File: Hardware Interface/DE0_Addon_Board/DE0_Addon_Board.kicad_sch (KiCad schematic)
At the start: 5 parts, among them J1 Conn_02x20_Odd_Even, J3 Raspberry PI GPIO, U1 IS61WV25616EDBLL

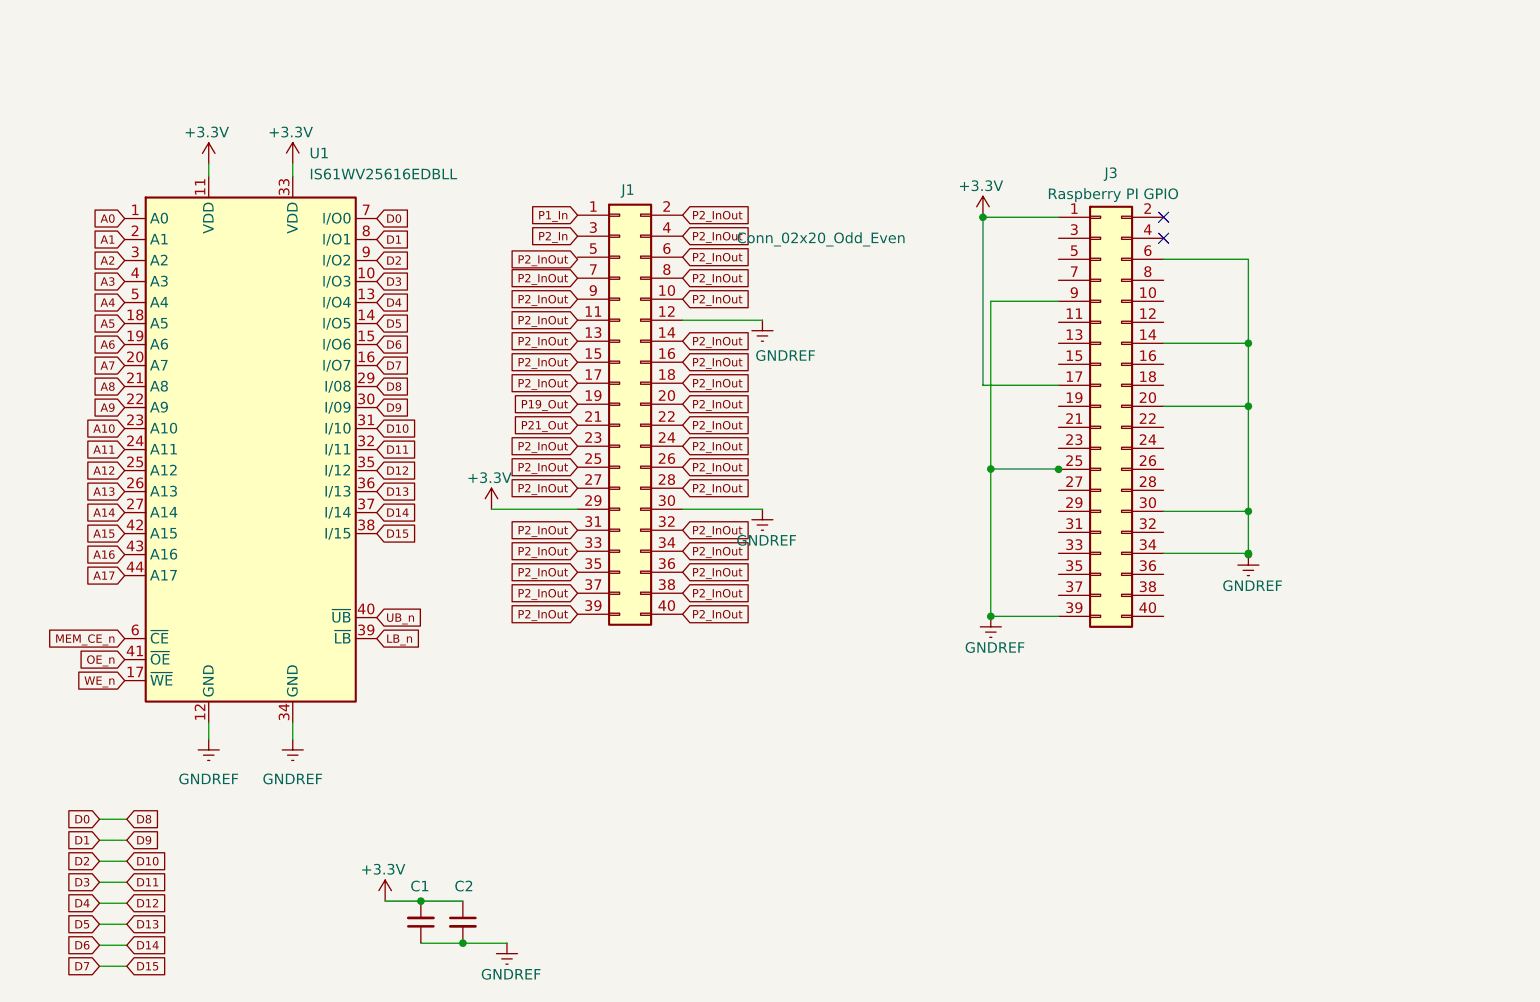
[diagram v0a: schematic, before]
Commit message: Addon-board changed to support Raspberry Pi in the GPIO connector
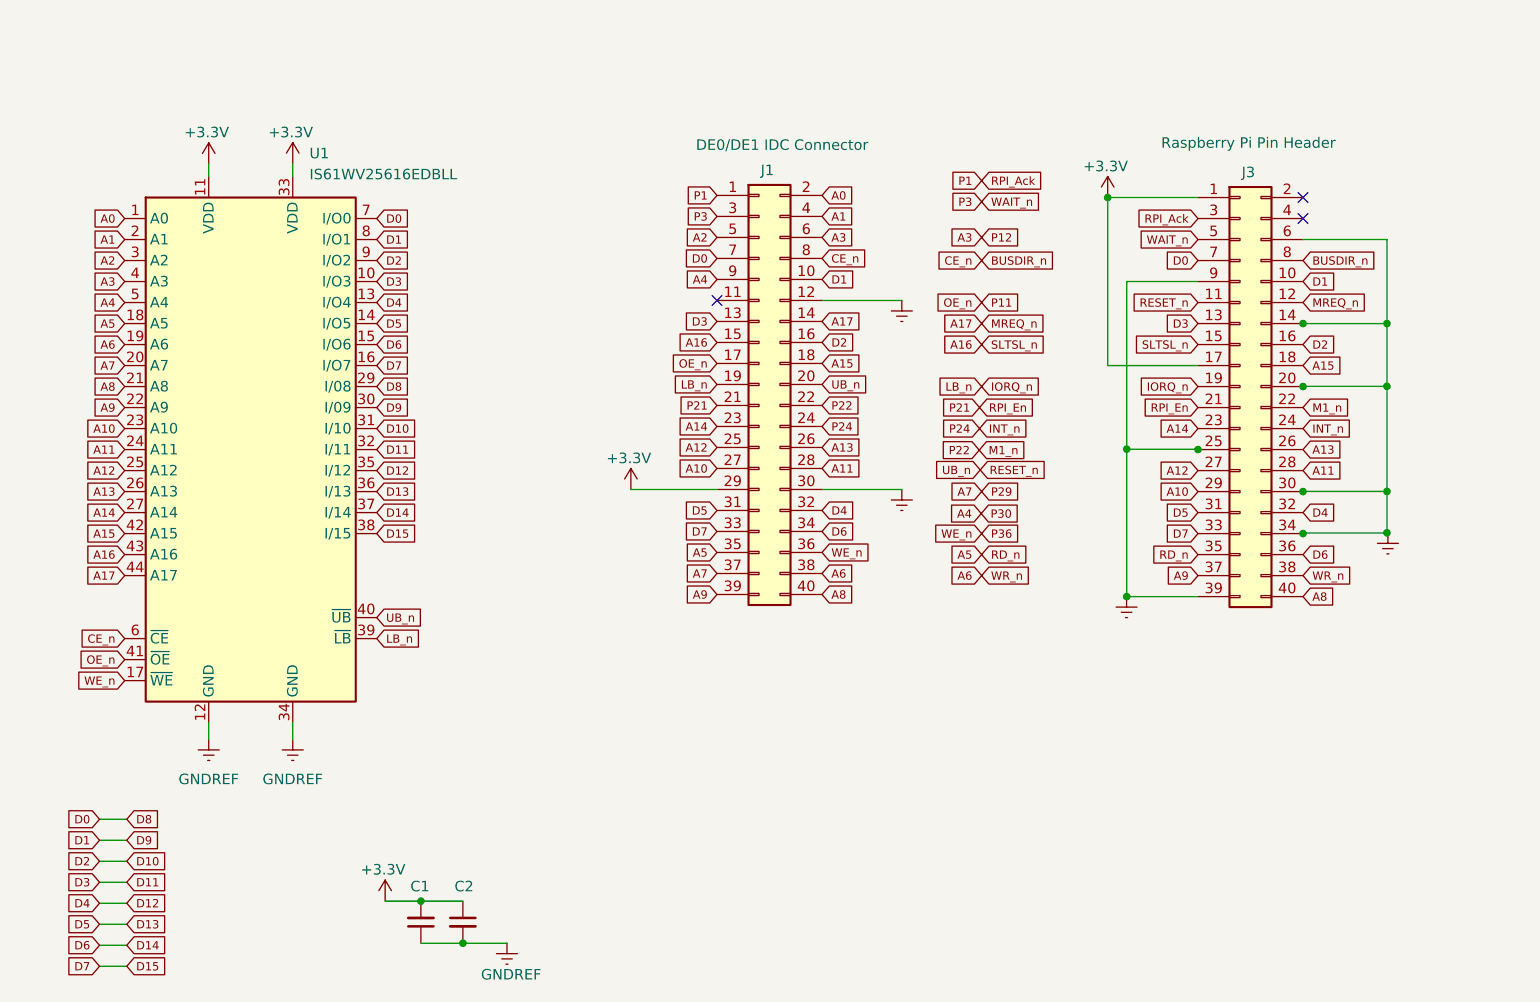
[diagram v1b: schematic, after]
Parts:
- J1: value Conn_02x20_Odd_Even -> DE0/DE1 IDC Connector
- J3: value Raspberry PI GPIO -> Raspberry Pi Pin Header; footprint Roni Footprints:PinSocket_2x20_P2.54mm_Vertical -> Connector_PinHeader_2.54mm:PinHeader_2x20_P2.54mm_Vertical
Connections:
- net LB_n is gone; now on net IORQ_n: U1.39 (~{LB})
- net MEM_CE_n is gone; now on net BUSDIR_n: U1.6 (~{CE})
- net P19_Out is gone; now on net IORQ_n: J1.19 (Pin_19)
- net P1_In is gone; now on net P1: J1.1 (Pin_1)
- net P21_Out is gone; now on net P21: J1.21 (Pin_21)
- net P2_In is gone; now on net P3: J1.3 (Pin_3)
- net UB_n is gone; now on net RESET_n: U1.40 (~{UB})
- net A0: now also J1.2 (Pin_2)
- net A1: now also J1.4 (Pin_4)
- net A10: now also J1.27 (Pin_27), J3.29 (Pin_29)
- net A11: now also J1.28 (Pin_28), J3.28 (Pin_28)
- net A12: now also J1.25 (Pin_25), J3.27 (Pin_27)
- net A13: now also J1.26 (Pin_26), J3.26 (Pin_26)
- net A14: now also J1.23 (Pin_23), J3.23 (Pin_23)
- net A15: now also J1.18 (Pin_18), J3.18 (Pin_18)
- net A16: now also J1.15 (Pin_15), J3.15 (Pin_15)
- net A17: now also J1.14 (Pin_14), J3.12 (Pin_12)
- net A2: now also J1.5 (Pin_5)
- net A3: now also J1.6 (Pin_6)
- net A4: now also J1.9 (Pin_9)
- net A5: now also J1.35 (Pin_35), J3.35 (Pin_35)
- net A6: now also J1.38 (Pin_38), J3.38 (Pin_38)
- net A7: now also J1.37 (Pin_37)
- net A8: now also J1.40 (Pin_40), J3.40 (Pin_40)
- net A9: now also J1.39 (Pin_39), J3.37 (Pin_37)
- net D0: now also J1.7 (Pin_7), J3.7 (Pin_7)
- net D1: now also J1.10 (Pin_10), J3.10 (Pin_10)
- net D10: now also J1.16 (Pin_16), J3.16 (Pin_16)
- net D11: now also J1.13 (Pin_13), J3.13 (Pin_13)
- net D12: now also J1.32 (Pin_32), J3.32 (Pin_32)
- net D13: now also J1.31 (Pin_31), J3.31 (Pin_31)
- net D14: now also J1.34 (Pin_34), J3.36 (Pin_36)
- net D15: now also J1.33 (Pin_33), J3.33 (Pin_33)
- net OE_n: now also J1.17 (Pin_17)
- net RESET_n: now reaches J3.11 (Pin_11)
- net RESET_n: now also J1.20 (Pin_20)
- net IORQ_n: now reaches J3.19 (Pin_19)
- net P21: now reaches J3.21 (Pin_21)
- net M1_n: now reaches J3.22 (Pin_22)
- net M1_n: now also J1.22 (Pin_22)
- net INT_n: now reaches J3.24 (Pin_24)
- net INT_n: now also J1.24 (Pin_24)
- net P1: now reaches J3.3 (Pin_3)
- net P3: now reaches J3.5 (Pin_5)
- net BUSDIR_n: now reaches J3.8 (Pin_8)
- net BUSDIR_n: now also J1.8 (Pin_8)
- removed net P2_InOut: J1.10 (Pin_10), J1.11 (Pin_11), J1.13 (Pin_13), J1.14 (Pin_14), J1.15 (Pin_15), J1.16 (Pin_16), J1.17 (Pin_17), J1.18 (Pin_18), J1.2 (Pin_2), J1.20 (Pin_20), J1.22 (Pin_22), J1.23 (Pin_23), J1.24 (Pin_24), J1.25 (Pin_25), J1.26 (Pin_26), J1.27 (Pin_27), J1.28 (Pin_28), J1.31 (Pin_31), J1.32 (Pin_32), J1.33 (Pin_33), J1.34 (Pin_34), J1.35 (Pin_35), J1.36 (Pin_36), J1.37 (Pin_37), J1.38 (Pin_38), J1.39 (Pin_39), J1.4 (Pin_4), J1.40 (Pin_40), J1.6 (Pin_6), J1.7 (Pin_7), J1.8 (Pin_8), J1.9 (Pin_9)
- net WE_n renamed P36
- net P36: now also J1.36 (Pin_36)
- no-connect marks 2 -> 3
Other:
- title: Terasic DE0 SRAM Addon Board -> Terasic DE0 SRAM & Raspberry Pi Addon Board
- moved on the sheet: J1, J3

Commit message: Changed footprint of SRAM decoupling capacitors to SMD 0603; Updated SRAM Addon for Rev.2
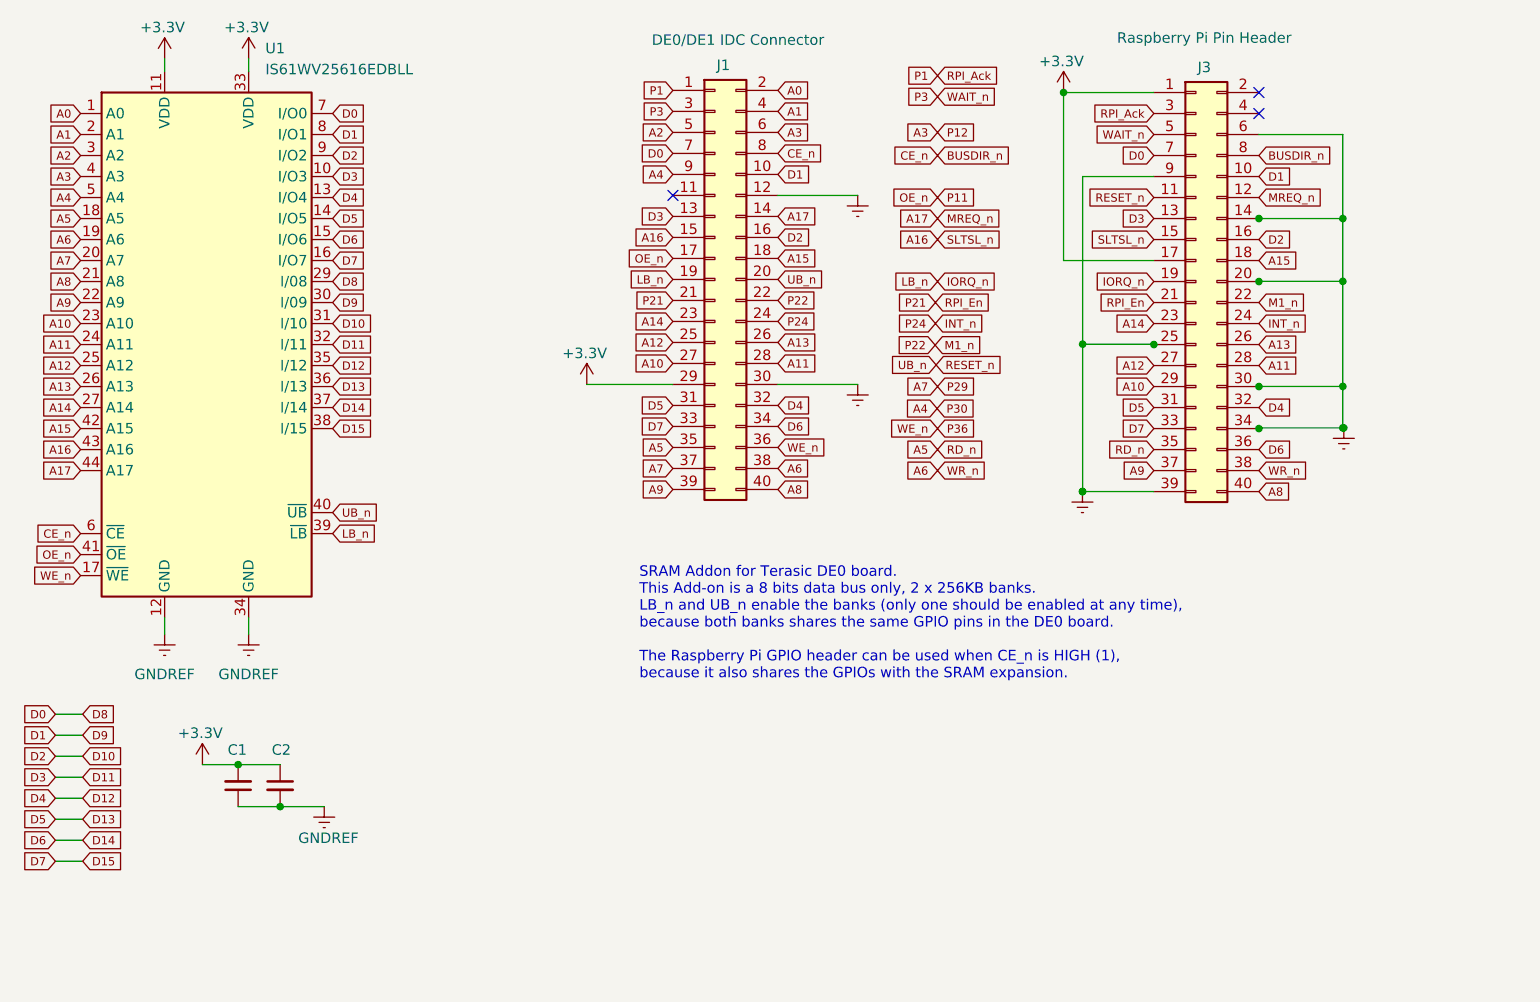
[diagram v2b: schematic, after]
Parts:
- C1, C2: footprint Capacitor_SMD:C_0402_1005Metric_Pad0.74x0.62mm_HandSolder -> Capacitor_SMD:C_0603_1608Metric_Pad1.08x0.95mm_HandSolder
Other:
- note added: "SRAM Addon for Terasic DE0 board. This Add-on is a 8 bits data bus only, 2 x 256KB banks. LB_n and UB_n enable the banks (only one should be enabled at any time), because both banks shares the same GPIO pins in the DE0 board. The Raspberry Pi GPIO header can be used when CE_n is HIGH (1), because it also shares the GPIOs with the SRAM expansion."
- moved on the sheet: C1, C2, J1, J3, U1

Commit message: Updated Add-On with silk in addresses for RPI
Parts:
- U1: value IS61WV25616EDBLL -> IS61LV25616AL-12T
